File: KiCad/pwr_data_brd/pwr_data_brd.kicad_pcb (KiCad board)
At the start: 2 copper layers, 33 parts, among them J2 9-12V From PoE Splitter, J3 3V Out For LNA, J4 5V Out For Filter Board, J7 USB_A, J8 USB_A, Q1 DMP4047LFDE-7, U13 MAX8510EXK30T, U14 TPS62133RGTR

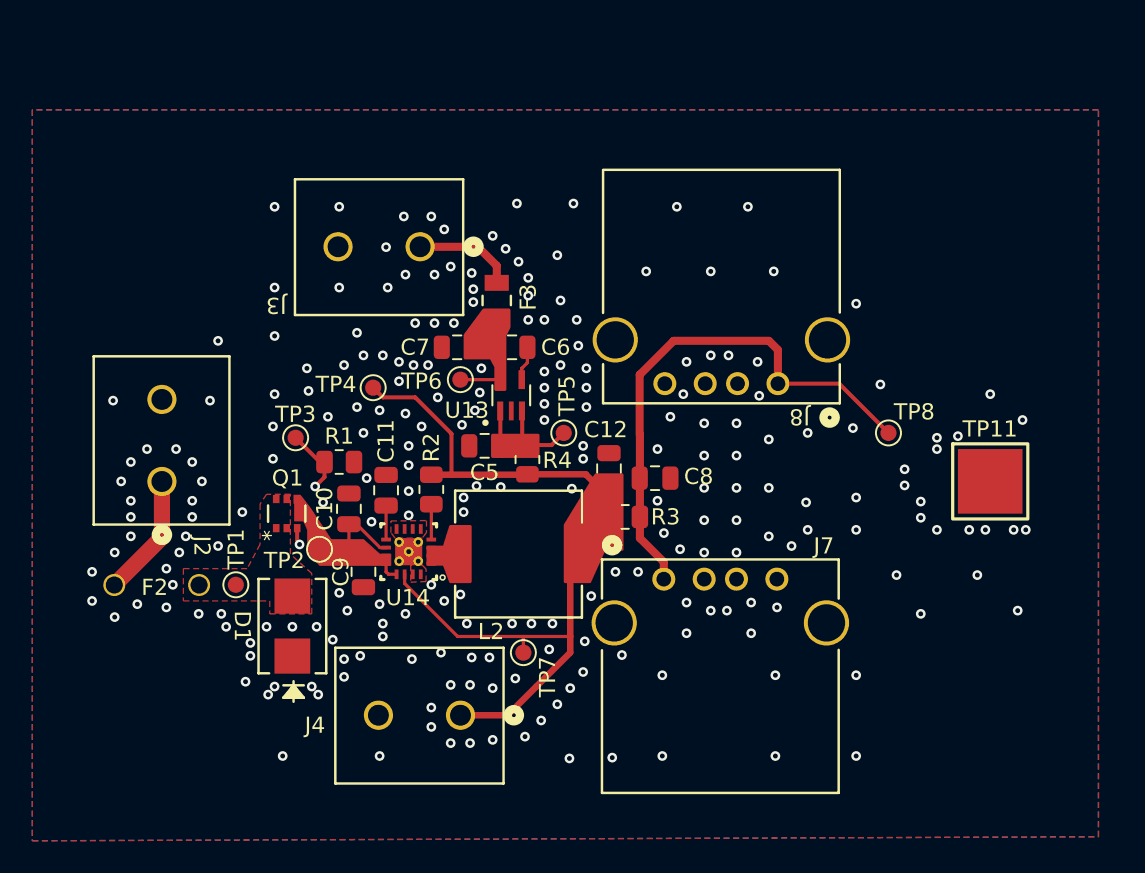
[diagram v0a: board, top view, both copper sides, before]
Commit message: Fix power board symbols and nets, added project specific libs
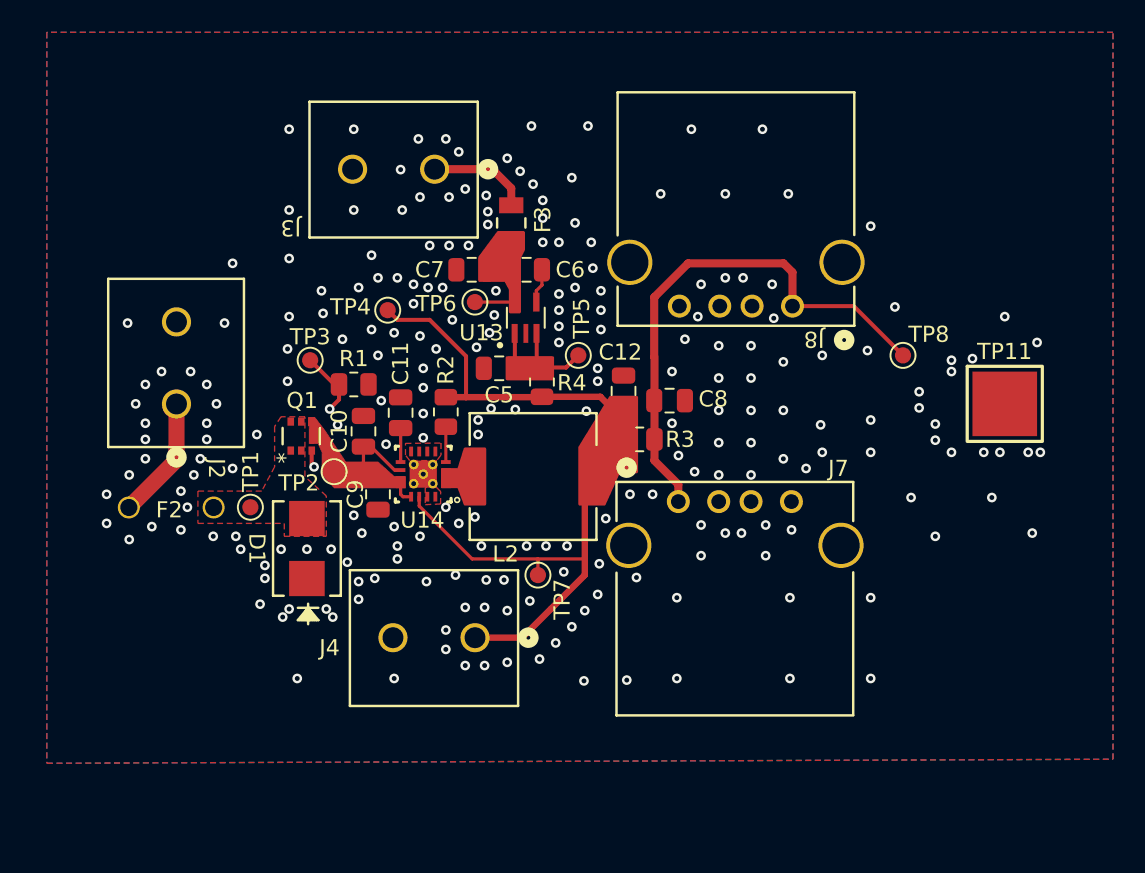
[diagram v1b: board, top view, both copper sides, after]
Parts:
- moved F2 4.88 mm to (122.0, 104.9)
- moved J3 4.88 mm to (138.0, 79.9)
- moved J4 4.88 mm to (140.5, 108.9)
- moved R4 4.88 mm to (144.6, 93.1)
- moved J2 4.88 mm to (122.0, 94.5)
- moved TP1 4.88 mm to (126.5, 100.8)
- moved Q1 4.88 mm to (129.7, 96.4)
- moved C10 4.88 mm to (133.6, 96.2)
- moved C11 4.88 mm to (135.8, 95.0)
- moved C12 4.88 mm to (149.7, 93.7)
- moved C6 4.88 mm to (143.7, 86.2)
- moved C7 4.88 mm to (140.2, 86.2)
- moved C8 4.88 mm to (152.5, 94.2)
- moved D1 4.88 mm to (130.1, 103.4)
- moved J8 4.88 mm to (160.1, 88.4)
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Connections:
- net /POWERDATA_GND renamed GND
- net /PowerDataDistribute/VDD renamed VDD
- net /PowerDataDistribute/VOUT_3V renamed /VOUT_3V
- net /PowerDataDistribute/VOUT_5V renamed /VOUT_5V
